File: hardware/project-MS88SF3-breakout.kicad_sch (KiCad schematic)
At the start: 27 parts, among them J1 Conn_02x05_Odd_Even, J2 S2B-PH-SM4-TB(LF)(SN), J3 USB4105-GF-A, J4 Conn_01x12_Male, J5 Conn_01x16_Male, U1 MS88SF3_NRF52840

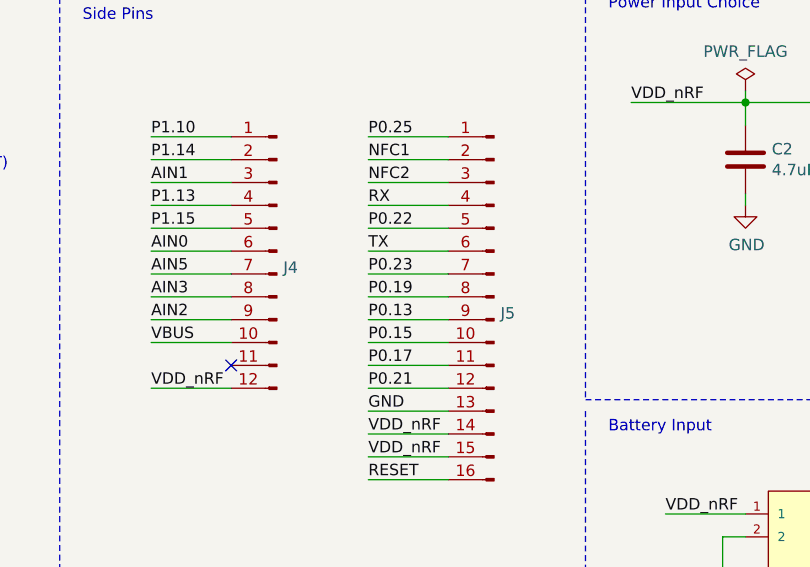
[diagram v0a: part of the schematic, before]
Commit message: Update obsolete connectors
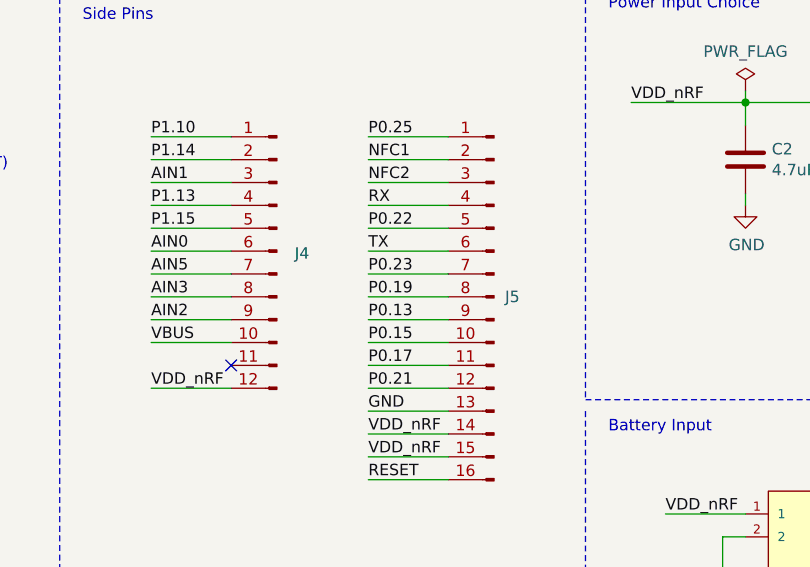
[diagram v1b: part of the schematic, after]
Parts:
- removed J4: Conn_01x12_Male, Connector_PinHeader_2.54mm:PinHeader_1x12_P2.54mm_Vertical, symbol Connector:Conn_01x12_Male
- removed J5: Conn_01x16_Male, Connector_PinHeader_2.54mm:PinHeader_1x16_P2.54mm_Vertical, symbol Connector:Conn_01x16_Male
- added J4: Conn_01x12_Pin, Connector_PinHeader_2.54mm:PinHeader_1x12_P2.54mm_Vertical, symbol Connector:Conn_01x12_Pin
- added J5: Conn_01x16_Pin, Connector_PinHeader_2.54mm:PinHeader_1x16_P2.54mm_Vertical, symbol Connector:Conn_01x16_Pin
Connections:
- net AIN0: now also J4.6 (Pin_6)
- net AIN1: now also J4.3 (Pin_3)
- net AIN2: now also J4.9 (Pin_9)
- net AIN3: now also J4.8 (Pin_8)
- net AIN5: now also J4.7 (Pin_7)
- net GND: now also J5.13 (Pin_13)
- net NFC1: now also J5.2 (Pin_2)
- net NFC2: now also J5.3 (Pin_3)
- net P0.13: now also J5.9 (Pin_9)
- net P0.15: now also J5.10 (Pin_10)
- net P0.17: now also J5.11 (Pin_11)
- net P0.19: now also J5.8 (Pin_8)
- net P0.21: now also J5.12 (Pin_12)
- net P0.22: now also J5.5 (Pin_5)
- net P0.23: now also J5.7 (Pin_7)
- net P0.25: now also J5.1 (Pin_1)
- net P1.10: now also J4.1 (Pin_1)
- net P1.13: now also J4.4 (Pin_4)
- net P1.14: now also J4.2 (Pin_2)
- net P1.15: now also J4.5 (Pin_5)
- net RESET: now also J5.16 (Pin_16)
- net RX: now also J5.4 (Pin_4)
- net TX: now also J5.6 (Pin_6)
- net VBUS: now also J4.10 (Pin_10)
- net VDD_nRF: now also J4.12 (Pin_12), J5.14 (Pin_14), J5.15 (Pin_15)
